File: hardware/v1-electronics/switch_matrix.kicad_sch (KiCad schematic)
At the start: 202 parts, among them SW1 SW_Push_45deg, SW10 SW_Push_45deg, SW11 SW_Push_45deg, SW12 SW_Push_45deg, SW13 SW_Push_45deg, SW14 SW_Push_45deg, SW15 SW_Push_45deg, SW16 SW_Push_45deg, SW17 SW_Push_45deg, SW18 SW_Push_45deg, SW19 SW_Push_45deg, SW2 SW_Push_45deg, SW20 SW_Push_45deg, SW23 SW_Push_45deg, SW24 SW_Push_45deg, SW25 SW_Push_45deg, SW26 SW_Push_45deg, SW27 SW_Push_45deg, SW28 SW_Push_45deg, SW29 SW_Push_45deg, SW3 SW_Push_45deg, SW30 SW_Push_45deg, SW31 SW_Push_45deg, SW32 SW_Push_45deg, SW33 SW_Push_45deg, SW34 SW_Push_45deg, SW37 SW_Push_45deg, SW38 SW_Push_45deg, SW39 SW_Push_45deg, SW4 SW_Push_45deg, SW40 SW_Push_45deg, SW41 SW_Push_45deg, SW42 SW_Push_45deg, SW43 SW_Push_45deg, SW44 SW_Push_45deg, SW45 SW_Push_45deg, SW46 SW_Push_45deg, SW47 SW_Push_45deg, SW48 SW_Push_45deg, SW5 SW_Push_45deg, SW51 SW_Push_45deg, SW52 SW_Push_45deg, SW53 SW_Push_45deg, SW54 SW_Push_45deg, SW55 SW_Push_45deg, SW56 SW_Push_45deg, SW57 SW_Push_45deg, SW58 SW_Push_45deg, SW59 SW_Push_45deg, SW6 SW_Push_45deg, SW60 SW_Push_45deg, SW61 SW_Push_45deg, SW62 SW_Push_45deg, SW63 SW_Push, SW66 SW_Push, SW67 SW_Push_45deg, SW68 SW_Push_45deg, SW69 SW_Push_45deg, SW70 SW_Push_45deg, SW71 SW_Push_45deg, SW72 SW_Push_45deg, SW9 SW_Push_45deg

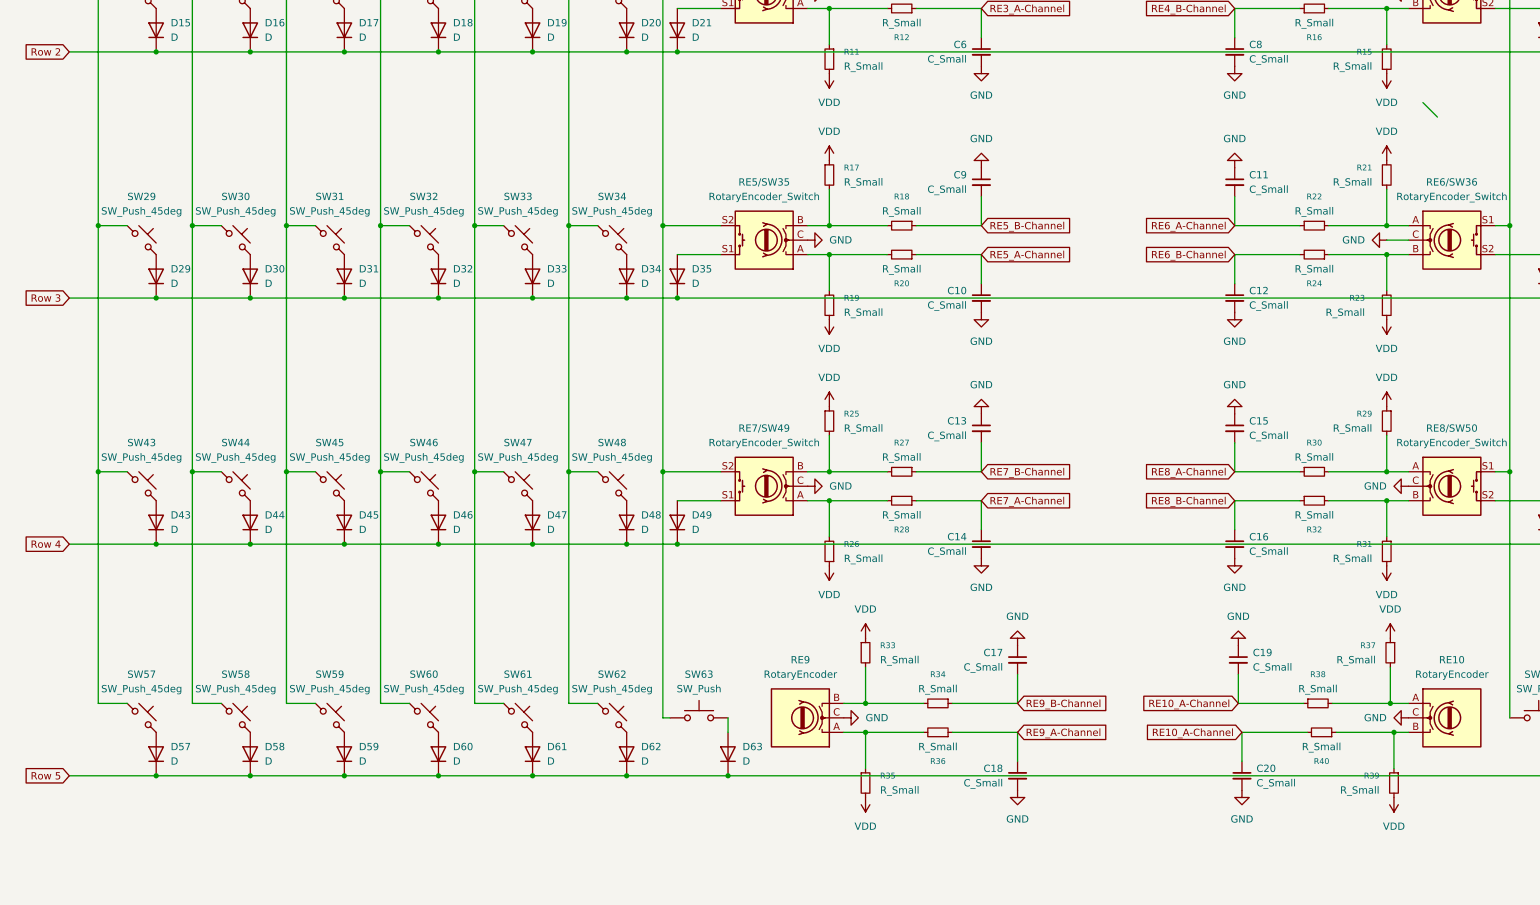
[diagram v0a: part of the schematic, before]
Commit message: feat(v1 hardware): add simple power circuitry
I've added simple power circuitry. It does not do everything I want but
it's a start.
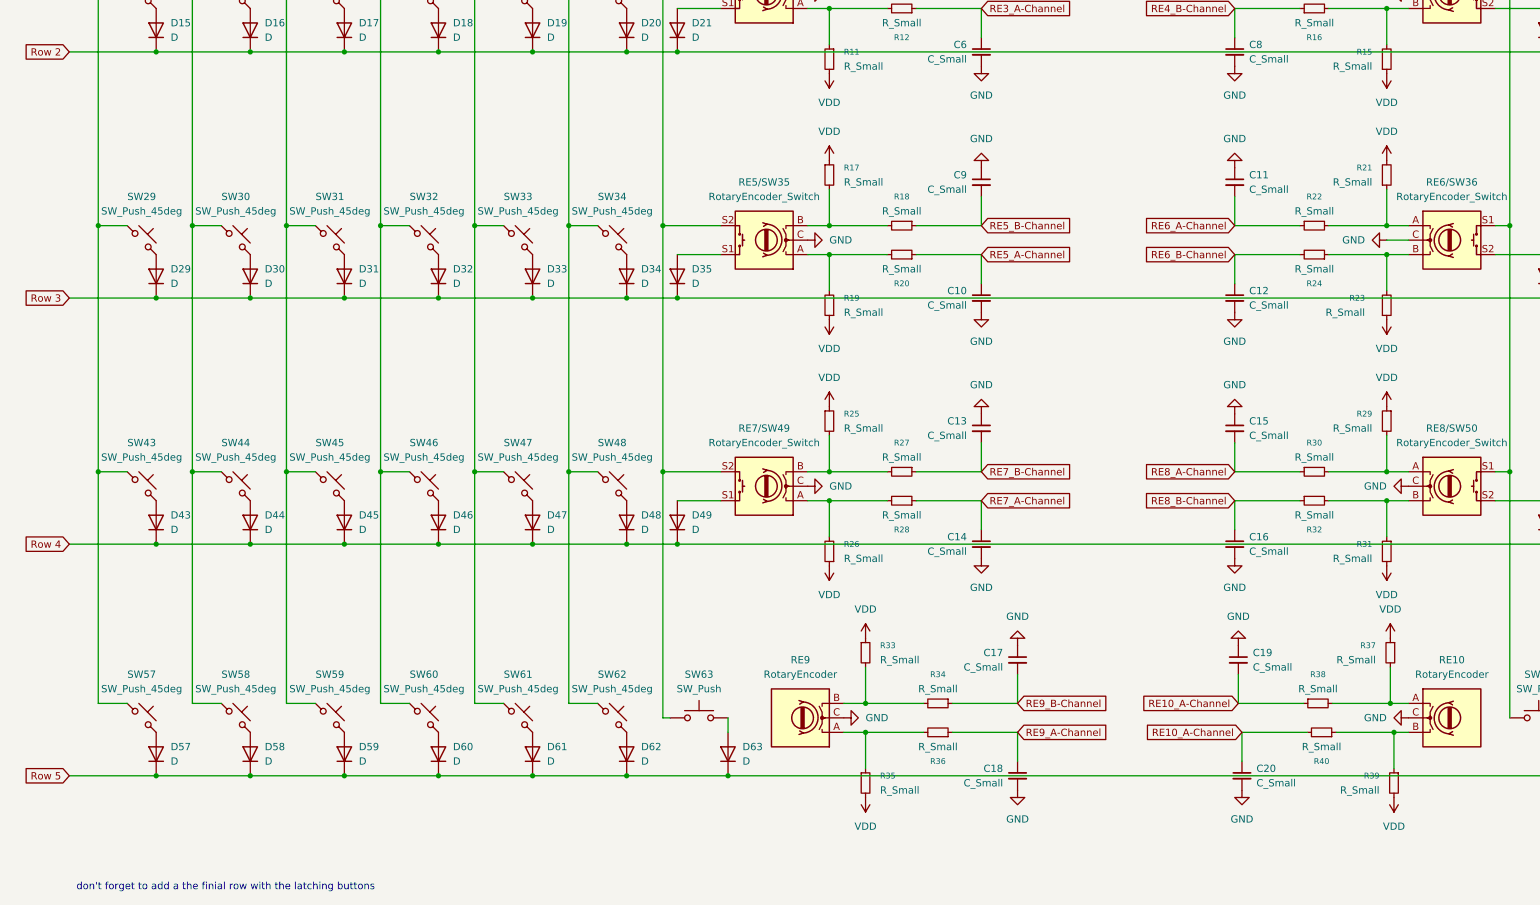
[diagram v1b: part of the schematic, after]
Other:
- note added: "don't forget to add a the finial row with the latching buttons"
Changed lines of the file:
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@@
 	(generator_version "10.0")
 	(paper "A3")
+	(text "don't forget to add a the finial row with the latching buttons"
+		(exclude_from_sim no)
+		(at 49.022 241.808 0)
+		(effects
+			(font
+				(size 1.27 1.27)
+			)
+		)
+	)
 	(junction
 		(at 252.73 87.63)
@@
 		(color 0 0 0 0)
 	)
-	(bus_entry
-		(at 259.08 104.14)
-		(size 2.54 2.54)
-		(stroke
-			(width 0)
-			(type default)
-		)
-	)
 	(wire

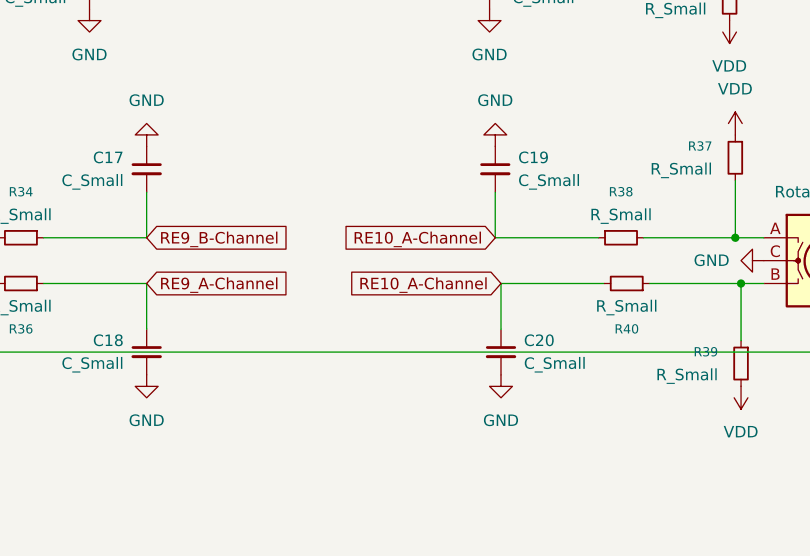
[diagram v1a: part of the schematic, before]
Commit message: feat(v1 hardware): start assigning pins on th mcu
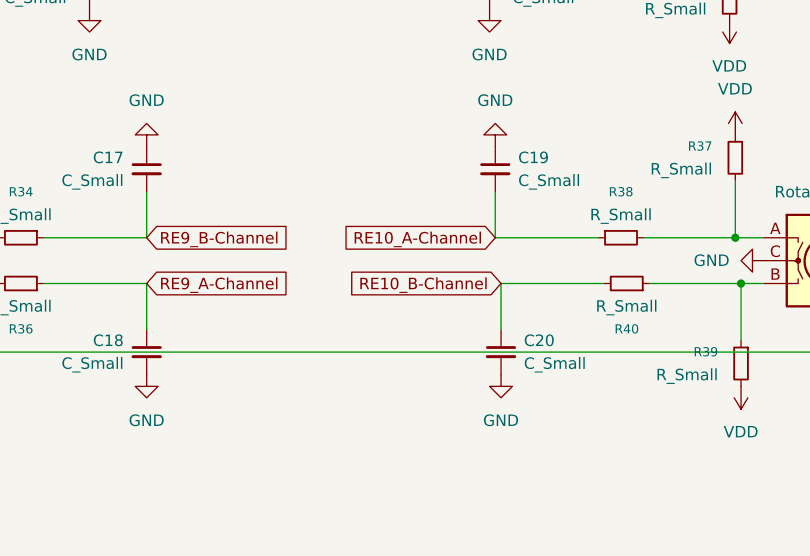
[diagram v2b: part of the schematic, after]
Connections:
- net RE10_A-Channel: no longer C20.1, R40.2
- new net RE10_B-Channel: C20.1, R40.2
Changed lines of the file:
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@@
 		)
 	)
-	(global_label "RE10_A-Channel"
+	(global_label "RE10_B-Channel"
 		(shape input)
 		(at 227.33 214.63 180)
@@
 		)
 		(property "Intersheetrefs" "${INTERSHEET_REFS}"
-			(at 208.2584 214.63 0)
+			(at 208.077 214.63 0)
 			(hide yes)
 			(show_name no)

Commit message: refactor(v1 hardware): add different charger ic & clean-up schematics
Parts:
- added D71, D72, D73, D74, D75, D76, D77, D78, D79, D80, D81, D82, D83, D84: D, symbol Device:D
- added SW21, SW22, SW35, SW36, SW49, SW50, SW64, SW65, SW7, SW73, SW74, SW75, SW76, SW8: SW_DIP_x01, symbol Switch:SW_DIP_x01
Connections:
- net Column 1: now also SW7.1
- net Column 10: now also SW65.1
- net Column 11: now also SW73.1
- net Column 12: now also SW74.1
- net Column 13: now also SW75.1
- net Column 14: now also SW76.1
- net Column 2: now also SW8.1
- net Column 3: now also SW21.1
- net Column 4: now also SW22.1
- net Column 5: now also SW35.1
- net Column 6: now also SW36.1
- net Column 7: now also SW49.1
- net Column 8: now also SW50.1
- net Column 9: now also SW64.1
- new net: D78.2 (A), SW50.2
- new net: D72.2 (A), SW8.2
- new net: D74.2 (A), SW22.2
- new net: D77.2 (A), SW49.2
- new net: D81.2 (A), SW73.2
- new net: D73.2 (A), SW21.2
- new net: D80.2 (A), SW65.2
- new net: D79.2 (A), SW64.2
- new net: D71.2 (A), SW7.2
- new net: D84.2 (A), SW76.2
- new net: D75.2 (A), SW35.2
- new net: D76.2 (A), SW36.2
- new net: D82.2 (A), SW74.2
- new net: D83.2 (A), SW75.2
- new net Row 6: D71.1 (K), D72.1 (K), D73.1 (K), D74.1 (K), D75.1 (K), D76.1 (K), D77.1 (K), D78.1 (K), D79.1 (K), D80.1 (K), D81.1 (K), D82.1 (K), D83.1 (K), D84.1 (K)
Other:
- note added: "Latch Row"
- note added: "Main Matrix"
- note removed: "don't forget to add a the finial row with the latching buttons"

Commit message: fix(v1 hardware): fixed the matrix circuit
the change in LED Matrix Driver results in a need to change how we
wire the matrix. this diff accounts for that.

i needed to use a script to rename labels.
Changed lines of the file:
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@@
 		)
 		(stroke
-			(width 0.5)
+			(width 1)
 			(type dash_dot_dot)
 		)
